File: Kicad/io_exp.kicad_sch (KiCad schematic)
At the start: 4 parts, among them U1801 MCP23S17_SO, U1802 74HC245

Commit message: Update schematic files to Kicad 6.
Had to fix some symbols which didn't have perfect matches in K6.
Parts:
- renumbered C1801 to C2001, C1802 to C2002, U1801 to U2001, U1802 to U2002
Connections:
- net +3V3 renamed +3.3V
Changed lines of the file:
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@@
   (symbol (lib_id "Neotron-Common-Hardware:MCP23S17_SO") (at 112.395 77.47 0) (unit 1)
     (in_bom yes) (on_board yes)
-    (property "Reference" "U1801" (id 0) (at 100.965 52.705 0))
+    (property "Reference" "U2001" (id 0) (at 100.965 52.705 0))
     (property "Value" "MCP23S17_SO" (id 1) (at 121.285 52.705 0))
     (property "Footprint" "Package_SO:SOIC-28W_7.5x17.9mm_P1.27mm" (id 2) (at 117.475 102.87 0)
@@
   (symbol (lib_id "74xx:74HC245") (at 153.67 92.71 0) (unit 1)
     (in_bom yes) (on_board yes)
-    (property "Reference" "U1802" (id 0) (at 147.32 75.565 0))
+    (property "Reference" "U2002" (id 0) (at 147.32 75.565 0))
     (property "Value" "74HC245" (id 1) (at 159.385 75.565 0))
     (property "Footprint" "Package_SO:SO-20_12.8x7.5mm_P1.27mm" (id 2) (at 153.67 92.71 0)
@@
   (symbol (lib_id "power:GND") (at 153.67 115.57 0) (unit 1)
     (in_bom yes) (on_board yes)
-    (property "Reference" "#PWR01805" (id 0) (at 153.67 121.92 0)
+    (property "Reference" "#PWR02005" (id 0) (at 153.67 121.92 0)
       (effects (font (size 1.27 1.27)) hide)
     )
@@
   (symbol (lib_id "power:GND") (at 139.7 115.57 0) (unit 1)
     (in_bom yes) (on_board yes)
-    (property "Reference" "#PWR01803" (id 0) (at 139.7 121.92 0)
+    (property "Reference" "#PWR02003" (id 0) (at 139.7 121.92 0)
       (effects (font (size 1.27 1.27)) hide)
     )
@@
     (pin "1")
   )
-  (symbol (lib_id "Neotron-Common-Hardware-rescue:+3.3V-power") (at 112.395 47.625 0) (unit 1)
-    (in_bom yes) (on_board yes)
-    (property "Reference" "#PWR01801" (id 0) (at 112.395 51.435 0)
+  (symbol (lib_id "power:+3.3V") (at 112.395 47.625 0) (unit 1)
+    (in_bom yes) (on_board yes)
+    (property "Reference" "#PWR02001" (id 0) (at 112.395 51.435 0)
       (effects (font (size 1.27 1.27)) hide)
     )
@@
     (pin "1")
   )
-  (symbol (lib_id "Neotron-Common-Hardware-rescue:+3.3V-power") (at 153.67 70.485 0) (unit 1)
-    (in_bom yes) (on_board yes)
-    (property "Reference" "#PWR01804" (id 0) (at 153.67 74.295 0)
+  (symbol (lib_id "power:+3.3V") (at 153.67 70.485 0) (unit 1)
+    (in_bom yes) (on_board yes)
+    (property "Reference" "#PWR02004" (id 0) (at 153.67 74.295 0)
       (effects (font (size 1.27 1.27)) hide)
     )
@@
   (symbol (lib_id "power:GND") (at 112.395 115.57 0) (unit 1)
     (in_bom yes) (on_board yes)
-    (property "Reference" "#PWR01802" (id 0) (at 112.395 121.92 0)
+    (property "Reference" "#PWR02002" (id 0) (at 112.395 121.92 0)
       (effects (font (size 1.27 1.27)) hide)
     )
@@
     (pin "1")
   )
-  (symbol (lib_id "Neotron-Common-Hardware-rescue:+3.3V-power") (at 200.66 57.15 0) (unit 1)
-    (in_bom yes) (on_board yes)
-    (property "Reference" "#PWR01806" (id 0) (at 200.66 60.96 0)
+  (symbol (lib_id "power:+3.3V") (at 200.66 57.15 0) (unit 1)
+    (in_bom yes) (on_board yes)
+    (property "Reference" "#PWR02006" (id 0) (at 200.66 60.96 0)
       (effects (font (size 1.27 1.27)) hide)
     )
@@
   (symbol (lib_id "power:GND") (at 200.66 69.85 0) (unit 1)
     (in_bom yes) (on_board yes)
-    (property "Reference" "#PWR01807" (id 0) (at 200.66 76.2 0)
+    (property "Reference" "#PWR02007" (id 0) (at 200.66 76.2 0)
       (effects (font (size 1.27 1.27)) hide)
     )
@@
   (symbol (lib_id "Device:C") (at 200.66 63.5 0) (unit 1)
     (in_bom yes) (on_board yes)
-    (property "Reference" "C1801" (id 0) (at 203.581 62.3316 0)
+    (property "Reference" "C2001" (id 0) (at 203.581 62.3316 0)
       (effects (font (size 1.27 1.27)) (justify left))
     )
@@
   (symbol (lib_id "Device:C") (at 212.725 63.5 0) (unit 1)
     (in_bom yes) (on_board yes)
-    (property "Reference" "C1802" (id 0) (at 215.646 62.3316 0)
+    (property "Reference" "C2002" (id 0) (at 215.646 62.3316 0)
       (effects (font (size 1.27 1.27)) (justify left))
     )

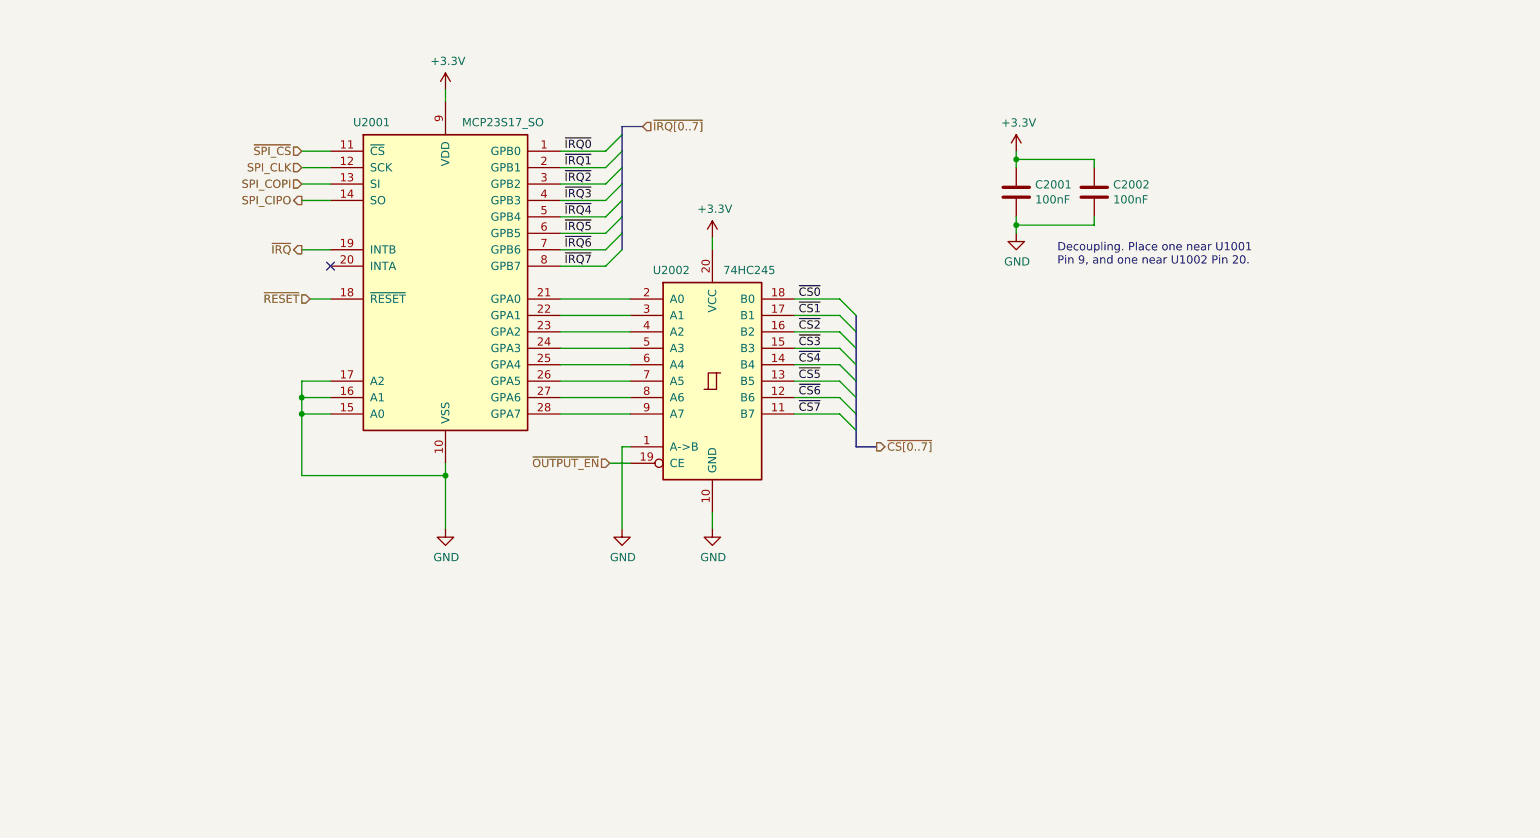
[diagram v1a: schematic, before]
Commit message: Imported sheets from Neotron Pico.
Standardised on +3V3 not +3.3V
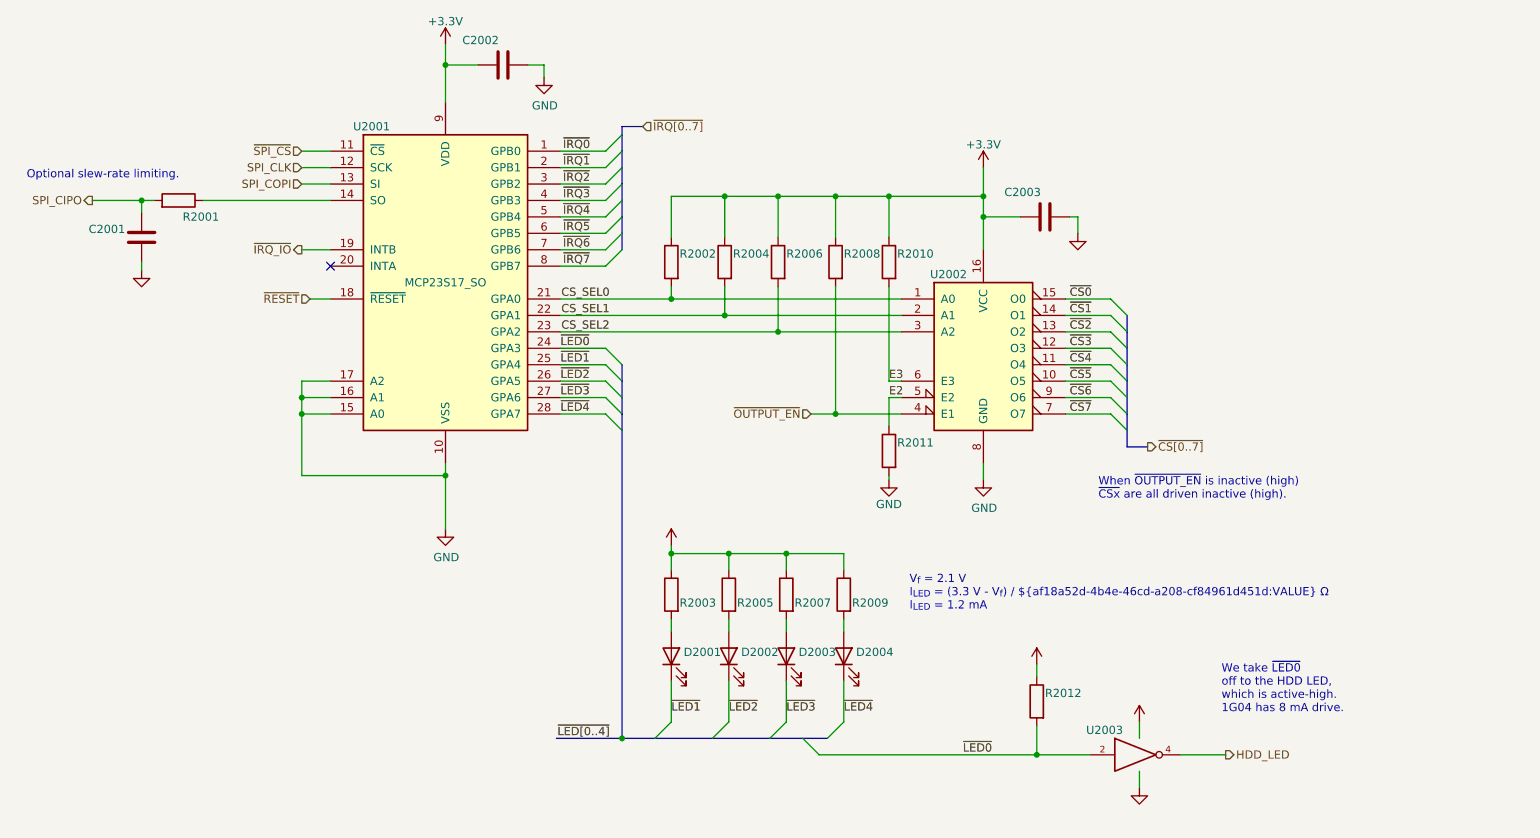
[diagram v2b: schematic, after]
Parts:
- removed U2002: 74HC245, Package_SO:SO-20_12.8x7.5mm_P1.27mm, symbol 74xx:74HC245
- added C2003: (no value), symbol Device:C
- added D2001, D2002, D2003, D2004: (no value), symbol Device:LED
- added R2001, R2002, R2003, R2004, R2005, R2006, R2007, R2008, R2009, R2010, R2011, R2012: (no value), symbol Device:R
- added U2002: (no value), symbol 74xx:74LS138
- added U2003: (no value), symbol 74xGxx:74AHC1G04
- C2001: value 100nF -> (none); footprint Capacitor_SMD:C_0805_2012Metric_Pad1.18x1.45mm_HandSolder -> (none); DNP 0 -> 1; LCSC Part# C49678 -> (none); MPN CPL-CAP-X7R-0805-100NF-50V -> (none); Manufacturer CPL -> (none); Tolerance X5R -> (none); Voltage 10V -> (none)
- C2002: value 100nF -> (none); footprint Capacitor_SMD:C_0805_2012Metric_Pad1.18x1.45mm_HandSolder -> (none); JLCPCB Collection (none) -> Basic; LCSC Part# C49678 -> C15850; MPN CPL-CAP-X7R-0805-100NF-50V -> CL21A106KAYNNNE; Manufacturer CPL -> Samsung; Voltage 10V -> 25V
- U2001: symbol Neotron-Common-Hardware:MCP23S17_SO -> Interface_Expansion:MCP23S17_SP; Digikey MCP23S17T-E/SOCT-ND -> MCP23S17-E/SP-ND; LCSC Part# C145413 -> (none); MPN MCP23S17T-E/SO -> MCP23S17-E/SP
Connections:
- net GND: now also C2003.2, R2011.2, U2002.8 (GND), U2003.3 (GND)
- net SPI_CIPO: now also C2001.1, R2001.2; no longer U2001.14 (SO)
- net ~{CS0}: now also U2002.15 (O0)
- net ~{CS1}: now also U2002.14 (O1)
- net ~{CS2}: now also U2002.13 (O2)
- net ~{CS3}: now also U2002.12 (O3)
- net ~{CS4}: now also U2002.11 (O4)
- net ~{CS5}: now also U2002.10 (O5)
- net ~{CS6}: now also U2002.9 (O6)
- net ~{CS7}: now also U2002.7 (O7)
- net ~{OUTPUT_EN}: now also R2008.2, U2002.4 (E1)
- net CS_SEL0: now reaches U2001.21 (GPA0)
- net CS_SEL0: now also R2002.2, U2002.1 (A0)
- net CS_SEL1: now reaches U2001.22 (GPA1)
- net CS_SEL1: now also R2004.2, U2002.2 (A1)
- net CS_SEL2: now reaches U2001.23 (GPA2)
- net CS_SEL2: now also R2006.2, U2002.3 (A2)
- net ~{LED0}: now reaches U2001.24 (GPA3)
- net ~{LED0}: now also R2012.2, U2003.2
- net ~{LED1}: now reaches U2001.25 (GPA4)
- net ~{LED1}: now also D2001.1 (K)
- net ~{LED2}: now reaches U2001.26 (GPA5)
- net ~{LED2}: now also D2002.1 (K)
- net ~{LED3}: now reaches U2001.27 (GPA6)
- net ~{LED3}: now also D2003.1 (K)
- net ~{LED4}: now reaches U2001.28 (GPA7)
- net ~{LED4}: now also D2004.1 (K)
- net +3.3V renamed +3V3
- net +3V3: now also C2003.1, R2002.1, R2003.1, R2004.1, R2005.1, R2006.1, R2007.1, R2008.1, R2009.1, R2010.1, R2012.1, U2002.16 (VCC), U2003.5 (VCC); no longer C2001.1
- net ~{IRQ} renamed ~{IRQ_IO}
- new net: R2001.1, U2001.14 (SO)
- new net: D2003.2 (A), R2007.2
- new net: D2001.2 (A), R2003.2
- new net: D2002.2 (A), R2005.2
- new net: D2004.2 (A), R2009.2
- new net E2: R2011.1, U2002.5 (E2)
- new net E3: R2010.2, U2002.6 (E3)
- new net HDD_LED: U2003.4
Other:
- note added: "Optional slew-rate limiting."
- note added: "V_{f} = 2.1 V I_{LED} = (3.3 V - V_{f}) / ${af18a52d-4b4e-46cd-a208-cf84961d451d:VALUE} Ω I_{LED} = 1.2 mA"
- note added: "We take ~{LED0} off to the HDD LED, which is active-high. 1G04 has 8 mA drive."
- note added: "When ~{OUTPUT_EN} is inactive (high) ~{CSx} are all driven inactive (high)."
- note removed: "Decoupling. Place one near U1001 Pin 9, and one near U1002 Pin 20."
- company: (none) -> https://neotron-compute.github.io
- title: (none) -> Neotron Bus Control

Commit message: Set missing footprints and update PCB
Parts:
- C2001: value (none) -> DNF; footprint (none) -> Capacitor_SMD:C_0805_2012Metric_Pad1.18x1.45mm_HandSolder
- C2002, C2003: value (none) -> 10u; footprint (none) -> Capacitor_SMD:C_0805_2012Metric_Pad1.18x1.45mm_HandSolder; JLCPCB Collection Basic -> (none); LCSC Part# C15850 -> (none); MPN CL21A106KAYNNNE -> (none); Manufacturer Samsung -> (none)
- D2001, D2002, D2003, D2004: value (none) -> LED; footprint (none) -> LED_SMD:LED_0805_2012Metric
- R2001: value (none) -> 0R; footprint (none) -> Resistor_SMD:R_0805_2012Metric_Pad1.20x1.40mm_HandSolder
- R2002, R2004, R2006, R2008, R2010, R2011, R2012: value (none) -> 10k; footprint (none) -> Resistor_SMD:R_0805_2012Metric_Pad1.20x1.40mm_HandSolder
- R2003, R2005, R2007, R2009: value (none) -> 1k; footprint (none) -> Resistor_SMD:R_0805_2012Metric_Pad1.20x1.40mm_HandSolder
- U2002: value (none) -> 74HC138; footprint (none) -> Package_SO:SOIC-16_3.9x9.9mm_P1.27mm
- U2003: value (none) -> 74AHC1G04; footprint (none) -> Package_TO_SOT_SMD:SOT-23-5_HandSoldering

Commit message: Re-imported from Neotron Pico v1.1.
This time I deleted the sheets from the top level and then re-added pointing at the new files. I also reset the PCB dimensions to match the Neotron Pico.

This seems to have done a better job importing footprints.
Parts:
- C502: renamed from C2002; JLCPCB Collection (none) -> Basic; LCSC Part# (none) -> C15850; MPN (none) -> CL21A106KAYNNNE; Manufacturer (none) -> Samsung
- C503: renamed from C2003; JLCPCB Collection (none) -> Basic; LCSC Part# (none) -> C15850; MPN (none) -> CL21A106KAYNNNE; Manufacturer (none) -> Samsung
- D501: renamed from D2001; footprint LED_SMD:LED_0805_2012Metric -> LED_SMD:LED_0805_2012Metric_Pad1.15x1.40mm_HandSolder
- D502: renamed from D2002; footprint LED_SMD:LED_0805_2012Metric -> LED_SMD:LED_0805_2012Metric_Pad1.15x1.40mm_HandSolder
- D503: renamed from D2003; footprint LED_SMD:LED_0805_2012Metric -> LED_SMD:LED_0805_2012Metric_Pad1.15x1.40mm_HandSolder
- D504: renamed from D2004; footprint LED_SMD:LED_0805_2012Metric -> LED_SMD:LED_0805_2012Metric_Pad1.15x1.40mm_HandSolder
- U501: renamed from U2001; value MCP23S17_SO -> MCP23S17_SP; footprint Package_SO:SOIC-28W_7.5x17.9mm_P1.27mm -> Package_DIP:DIP-28_W7.62mm
- renumbered C2001 to C501, R2001 to R501, R2002 to R502, R2003 to R503, R2004 to R504, R2005 to R505, R2006 to R506, R2007 to R507, R2008 to R508, R2009 to R509, R2010 to R510, R2011 to R511, R2012 to R512, U2002 to U502, U2003 to U503
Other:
- company: https://neotron-compute.github.io -> https://neotron-compute.github.io/
